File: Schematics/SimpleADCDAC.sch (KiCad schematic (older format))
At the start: 87 parts, among them CN701 COAX, CN702 COAX, P701 CONN_02X05, P702 CONN_2x1, P703 CONN_02X05, P704 CONN_3x1, P705 CONN_3x1, U701 IC-REG-LM317-TO220, U702 IC-DAC-WM8501, U703 IC-ADC-WM8783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

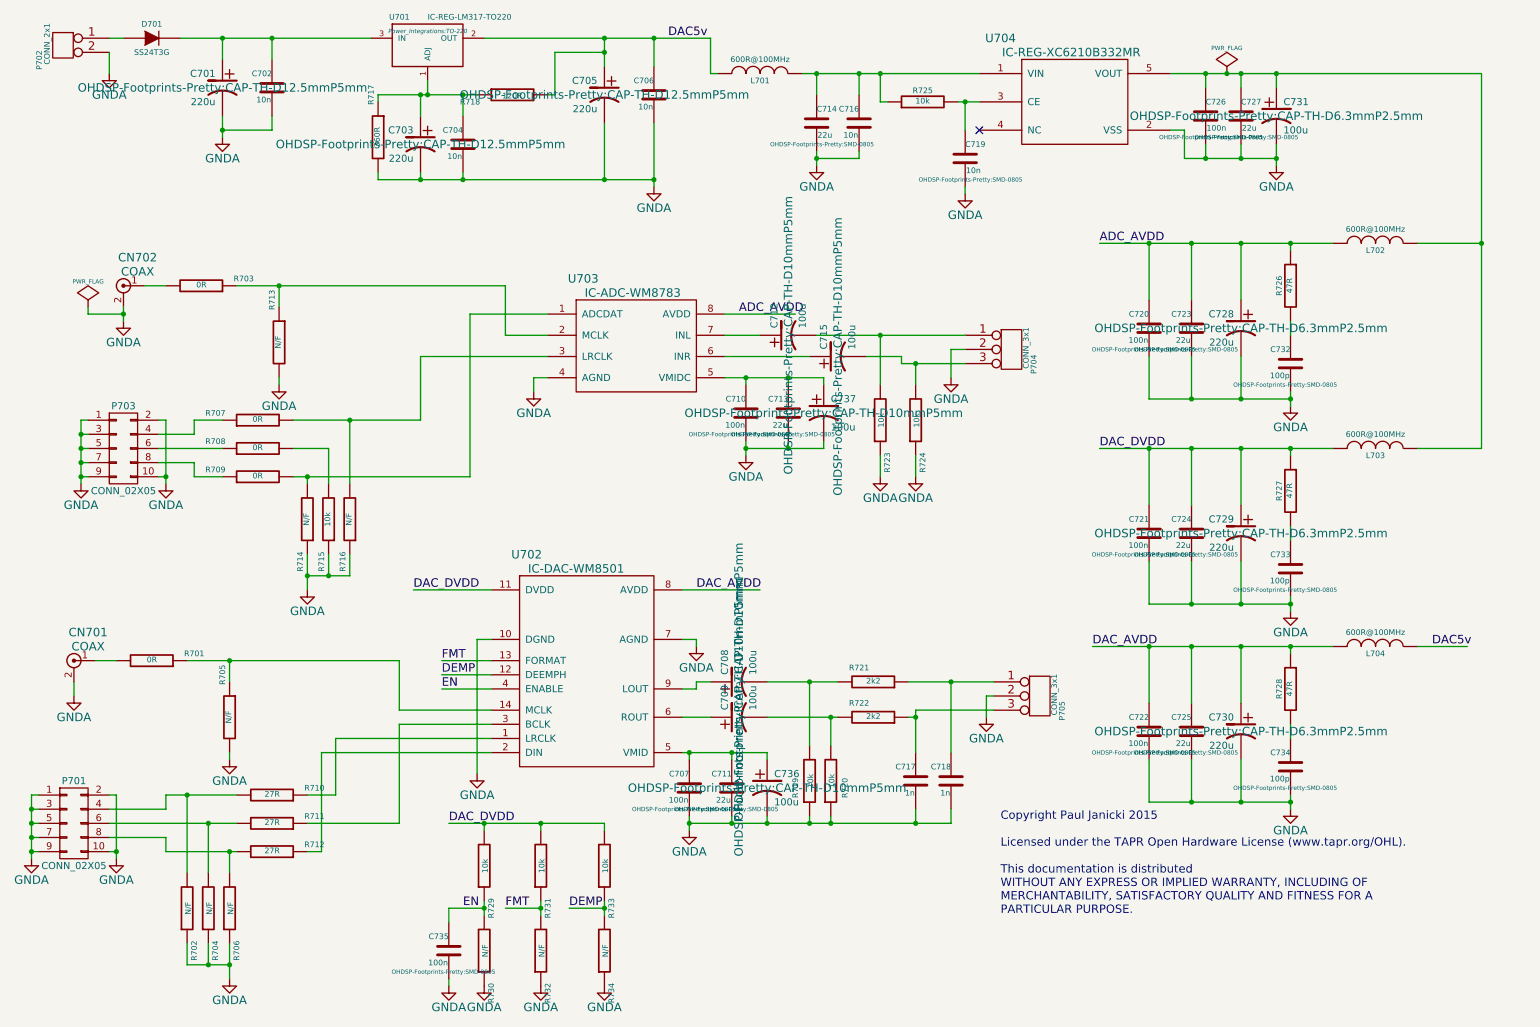
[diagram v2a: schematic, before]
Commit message: PCB work, added DAC/ADC
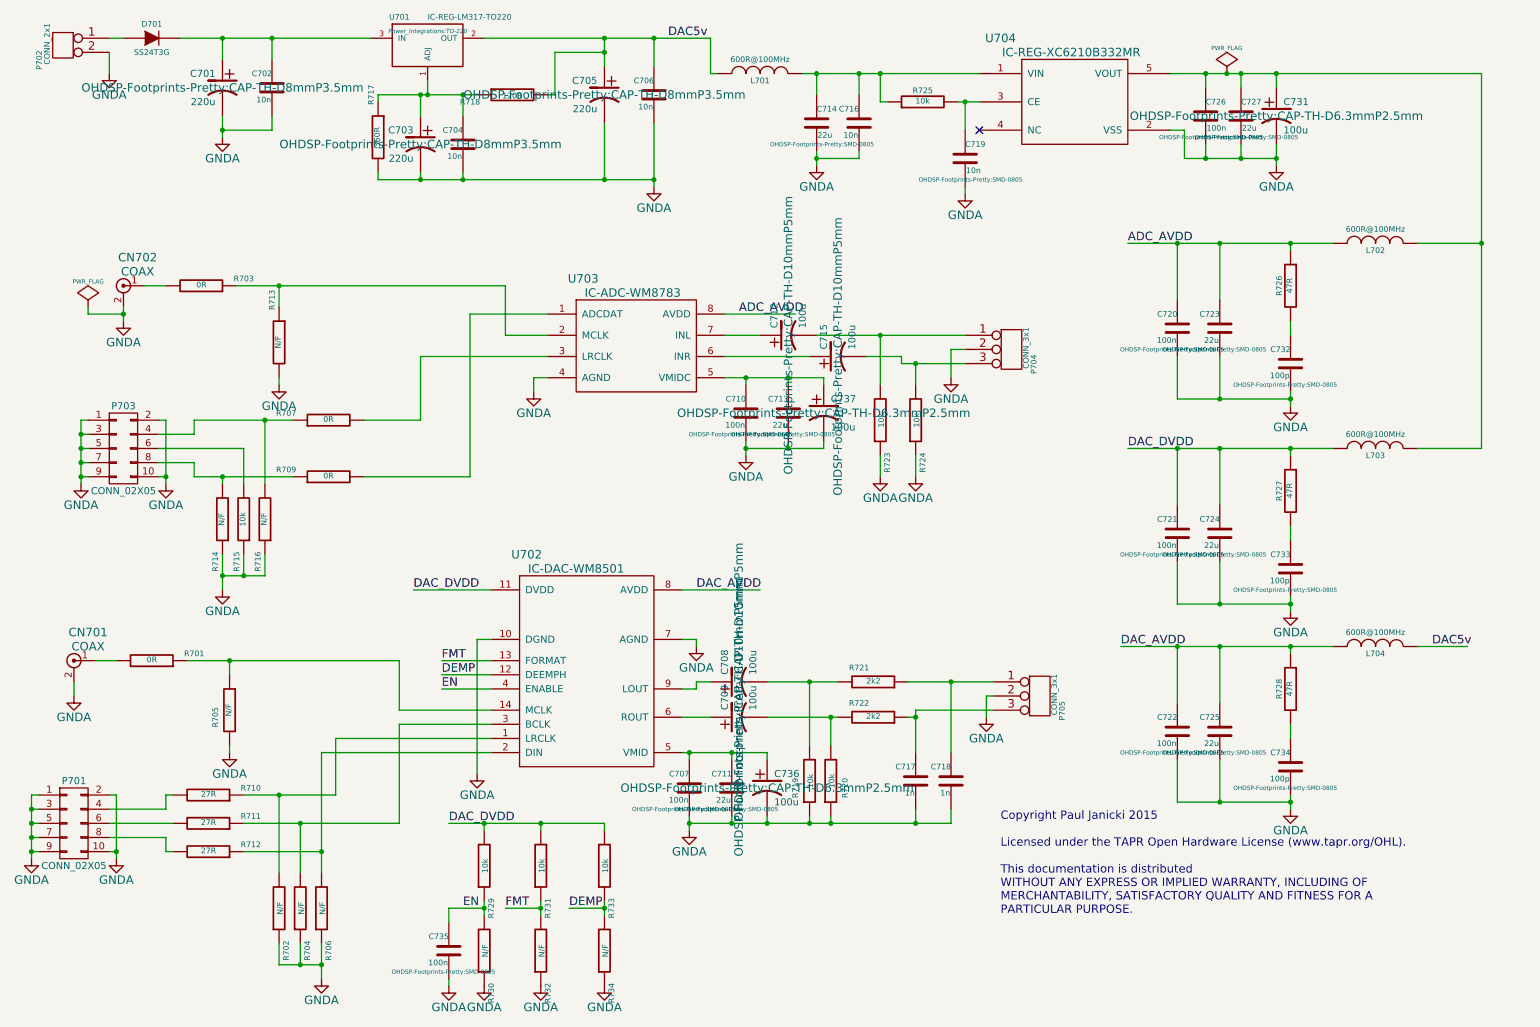
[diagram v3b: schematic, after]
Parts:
- removed C728, C729, C730: 220u, OHDSP-Footprints-Pretty:CAP-TH-D6.3mmP2.5mm, symbol CP1
- removed R708: 0R, OHDSP-Footprints-Pretty:SMD-0805, symbol R
- C701, C703, C705: footprint OHDSP-Footprints-Pretty:CAP-TH-D12.5mmP5mm -> OHDSP-Footprints-Pretty:CAP-TH-D8mmP3.5mm
- C717, C718: footprint OHDSP-Footprints-Pretty:CAP_TH_5mm -> OHDSP-Footprints-Pretty:SMD-0805
- C736, C737: footprint OHDSP-Footprints-Pretty:CAP-TH-D10mmP5mm -> OHDSP-Footprints-Pretty:CAP-TH-D6.3mmP2.5mm
- U702: footprint (none) -> OHDSP-Footprints-Pretty:IC_SOIC_14
- U703: footprint (none) -> OHDSP-Footprints-Pretty:IC_SOIC_8
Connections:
- net at R709.2, U703.1 (ADCDAT): no longer R714.2
- net at R707.2, U703.3 (LRCLK): no longer R716.2
- net at R710.1, U702.1 (LRCLK): now also R702.2
- net at R712.1, U702.2 (DIN): now also R706.2
- net at R711.1, U702.3 (BCLK): now also R704.2
- net at R715.2: now also P703.6 (P6)
- net at P703.4 (P4), R707.1: now also R716.2
- net at P703.8 (P8), R709.1: now also R714.2
- net at P701.4 (P4), R710.2: no longer R702.2
- net at P701.8 (P8), R712.2: no longer R706.2
- net at P701.6 (P6), R711.2: no longer R704.2
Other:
- moved on the sheet: C720, C721, C722, C723, C724, C725, R702, R704, R705, R706, R707, R709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
